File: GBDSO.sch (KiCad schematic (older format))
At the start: 71 parts, among them J1 MJ-3523-SMT-TR, J2 MJ-3523-SMT-TR, J3 Conn_01x32, P1 100k, P2 100k, SW1 SW_SPDT, SW2 SW_SPDT, U1 TL062, U2 DS1267_SOIC, U3 TL062, U4 MAX114CAG, U5 74HC175D, U6 74HC138D, U7 AT27C256R, U8 TLC272, U9 MAX828

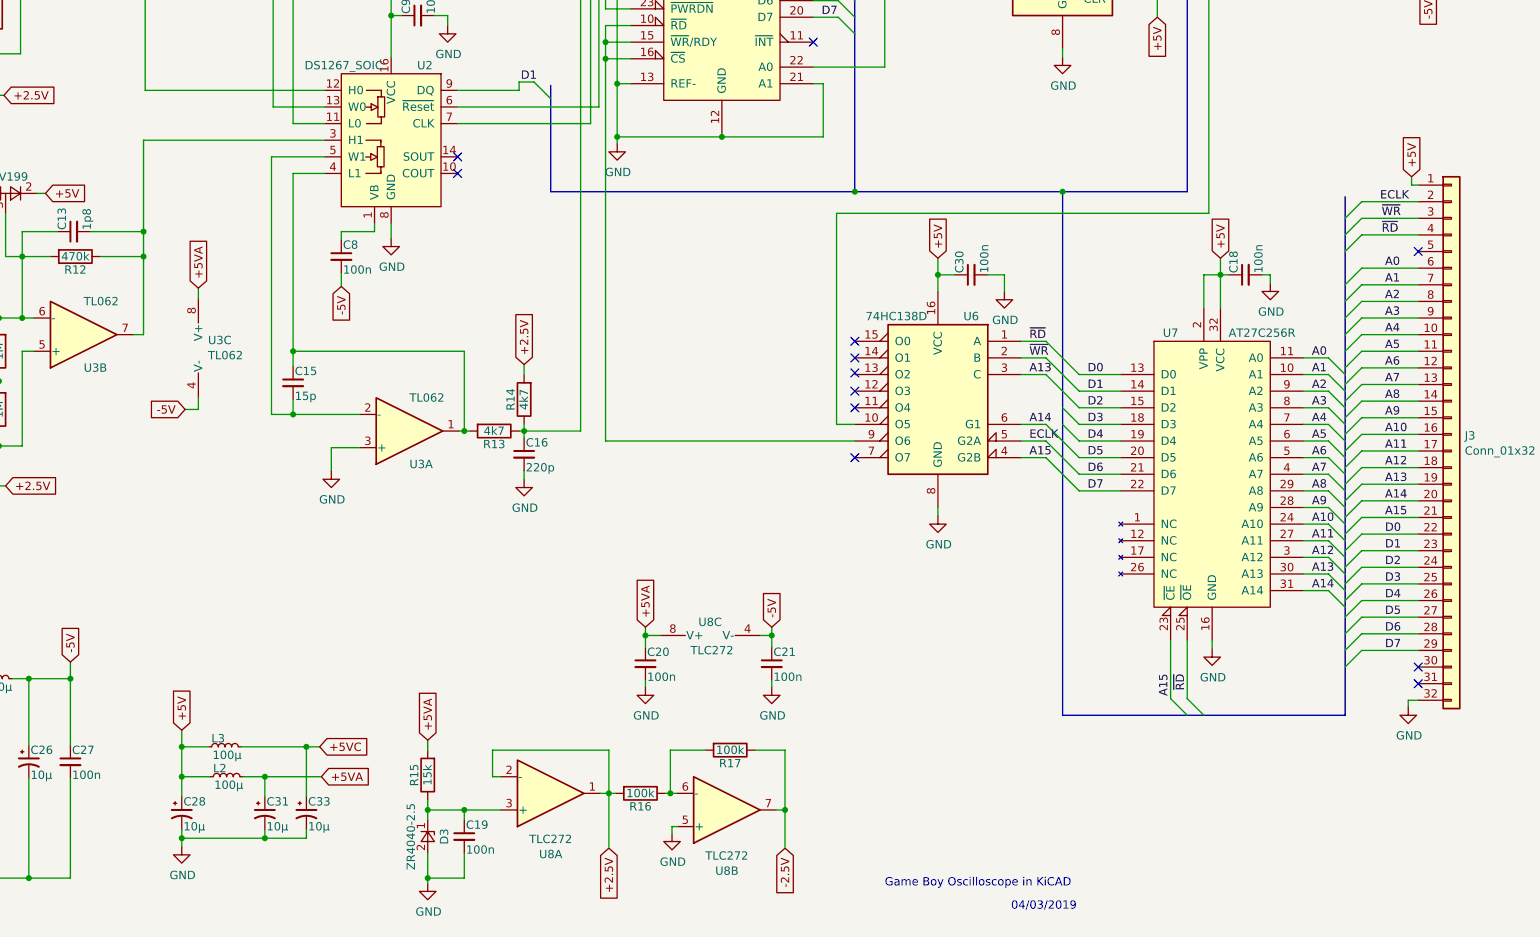
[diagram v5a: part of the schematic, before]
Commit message: added jumpers to the schematic and pcb so that the EPROM can be programmed on the cartridge
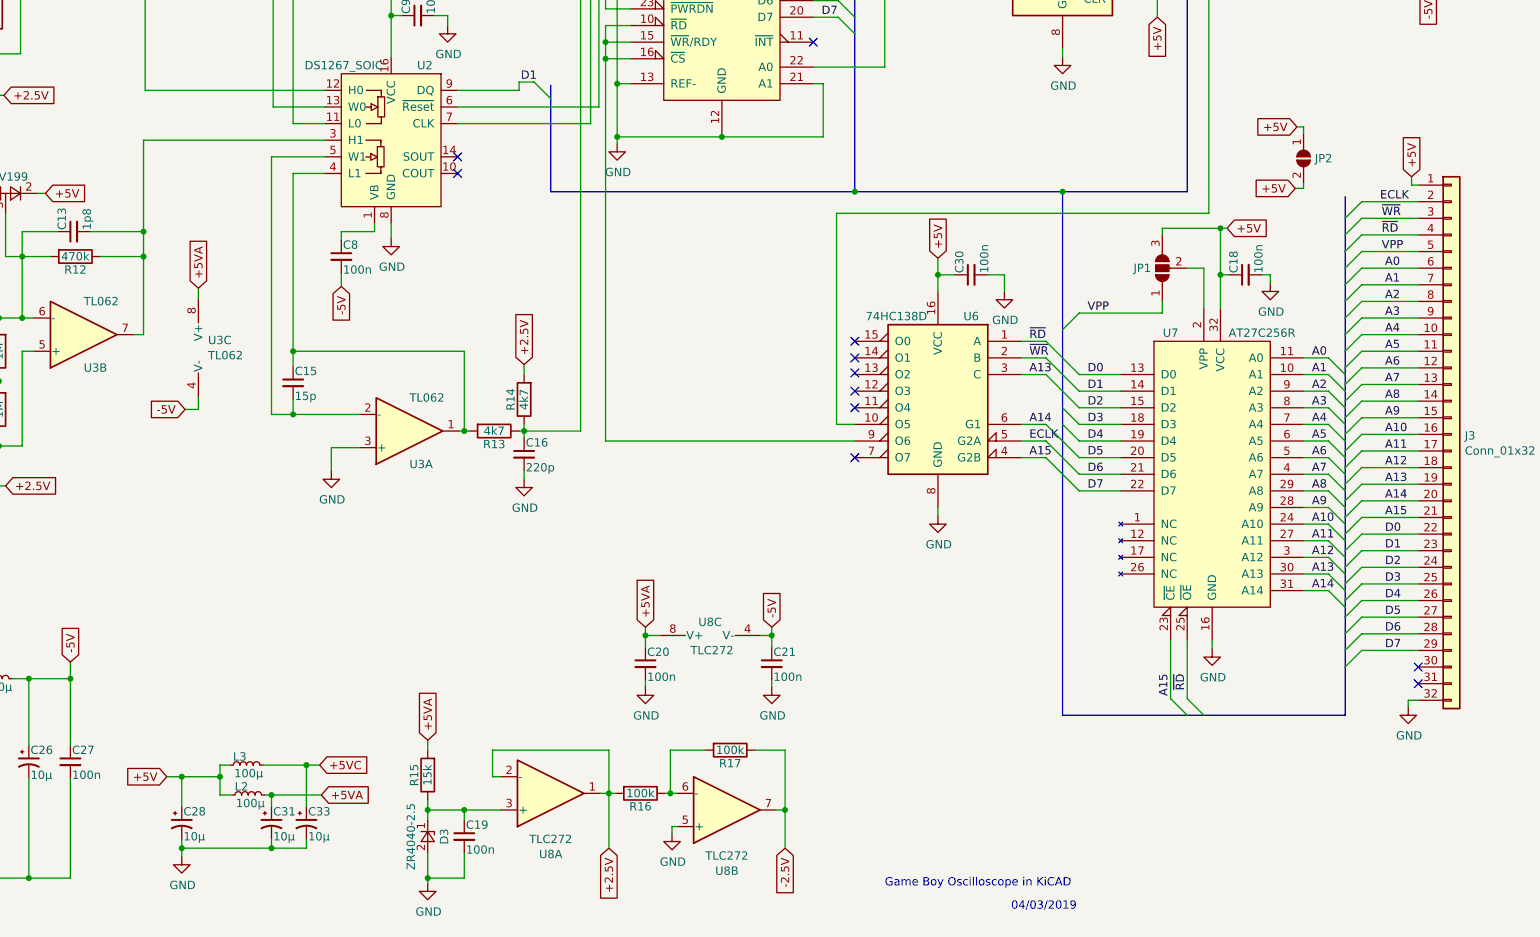
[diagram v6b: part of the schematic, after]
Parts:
- added JP1: SolderJumper_3_Open, Jumper:SolderJumper-3_P1.3mm_Open_RoundedPad1.0x1.5mm_NumberLabels, symbol Jumper:SolderJumper_3_Open
- added JP2: SolderJumper_2_Open, Jumper:SolderJumper-2_P1.3mm_Open_TrianglePad1.0x1.5mm, symbol Jumper:SolderJumper_2_Open
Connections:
- net +5V: now also JP1.3 (B), JP2.1 (A), JP2.2 (B); no longer U7.2 (VPP)
- net VPP: now reaches J3.5 (Pin_5)
- net VPP: now also JP1.1 (A)
- new net: JP1.2 (C), U7.2 (VPP)
- no-connect marks 18 -> 17
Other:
- moved on the sheet: C28, C31, C33, L2, L3
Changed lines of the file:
@@
 L Device:CP1_Small C28
 U 1 1 5C618C17
-P 3150 7050
-F 0 "C28" H 3160 7120 50  0000 L CNN
-F 1 "10µ" H 3160 6970 50  0000 L CNN
-F 2 "Capacitor_SMD:C_1206_3216Metric" H 3150 7050 50  0001 C CNN
-F 3 "" H 3150 7050 50  0001 C CNN
-	1    3150 7050
+P 3150 7110
+F 0 "C28" H 3160 7180 50  0000 L CNN
+F 1 "10µ" H 3160 7030 50  0000 L CNN
+F 2 "Capacitor_SMD:C_1206_3216Metric" H 3150 7110 50  0001 C CNN
+F 3 "" H 3150 7110 50  0001 C CNN
+	1    3150 7110
 	1    0    0    -1
 $EndComp
@@
 L Device:CP1_Small C31
 U 1 1 5C618CCF
-P 3650 7050
-F 0 "C31" H 3660 7120 50  0000 L CNN
-F 1 "10µ" H 3660 6970 50  0000 L CNN
-F 2 "Capacitor_SMD:C_1206_3216Metric" H 3650 7050 50  0001 C CNN
-F 3 "" H 3650 7050 50  0001 C CNN
-	1    3650 7050
+P 3690 7110
+F 0 "C31" H 3700 7180 50  0000 L CNN
+F 1 "10µ" H 3700 7030 50  0000 L CNN
+F 2 "Capacitor_SMD:C_1206_3216Metric" H 3690 7110 50  0001 C CNN
+F 3 "" H 3690 7110 50  0001 C CNN
+	1    3690 7110
 	1    0    0    -1
 $EndComp
@@
 L Device:CP1_Small C33
 U 1 1 5C618D96
-P 3900 7050
-F 0 "C33" H 3910 7120 50  0000 L CNN
-F 1 "10µ" H 3910 6970 50  0000 L CNN
-F 2 "Capacitor_SMD:C_1206_3216Metric" H 3900 7050 50  0001 C CNN
-F 3 "" H 3900 7050 50  0001 C CNN
-	1    3900 7050
+P 3900 7110
+F 0 "C33" H 3910 7180 50  0000 L CNN
+F 1 "10µ" H 3910 7030 50  0000 L CNN
+F 2 "Capacitor_SMD:C_1206_3216Metric" H 3900 7110 50  0001 C CNN
+F 3 "" H 3900 7110 50  0001 C CNN
+	1    3900 7110
 	1    0    0    -1
 $EndComp
@@
 L Device:L_Small L2
 U 1 1 5C619CA4
-P 3420 6830
-F 0 "L2" V 3470 6830 50  0000 L CNN
-F 1 "100µ" V 3370 6730 50  0000 L CNN
-F 2 "Inductor_SMD:L_1206_3216Metric" H 3420 6830 50  0001 C CNN
-F 3 "" H 3420 6830 50  0001 C CNN
-	1    3420 6830
+P 3550 6940
+F 0 "L2" V 3600 6940 50  0000 L CNN
+F 1 "100µ" V 3500 6840 50  0000 L CNN
+F 2 "Inductor_SMD:L_1206_3216Metric" H 3550 6940 50  0001 C CNN
+F 3 "" H 3550 6940 50  0001 C CNN
+	1    3550 6940
 	0    -1   -1   0
 $EndComp
@@
 L Device:L_Small L3
 U 1 1 5C619D6A
-P 3410 6650
-F 0 "L3" V 3460 6650 50  0000 L CNN
-F 1 "100µ" V 3360 6550 50  0000 L CNN
-F 2 "Inductor_SMD:L_1206_3216Metric" H 3410 6650 50  0001 C CNN
-F 3 "" H 3410 6650 50  0001 C CNN
-	1    3410 6650
+P 3540 6760
+F 0 "L3" V 3590 6760 50  0000 L CNN
+F 1 "100µ" V 3490 6660 50  0000 L CNN
+F 2 "Inductor_SMD:L_1206_3216Metric" H 3540 6760 50  0001 C CNN
+F 3 "" H 3540 6760 50  0001 C CNN
+	1    3540 6760
 	0    -1   -1   0
 $EndComp
@@
 	9400 3810 9400 4010
 Wire Wire Line
-	9300 3810 9400 3810
-Wire Wire Line
-	9300 3810 9300 4010
-Wire Wire Line
-	3510 6650 3900 6650
-Wire Wire Line
-	3900 6650 3900 6950
-Wire Wire Line
-	3150 7150 3150 7200
-Wire Wire Line
-	3150 7200 3650 7200
-Wire Wire Line
-	3650 7200 3650 7150
+	3640 6760 3900 6760
+Wire Wire Line
+	3900 6760 3900 7010
+Wire Wire Line
+	3150 7210 3150 7260
+Wire Wire Line
+	3150 7260 3690 7260
+Wire Wire Line
+	3690 7260 3690 7210
 $Comp
 L power:GND #PWR0106
 U 1 1 5C6DF12D
-P 3150 7250
-F 0 "#PWR0106" H 3150 7000 50  0001 C CNN
-F 1 "GND" H 3155 7077 50  0000 C CNN
-F 2 "" H 3150 7250 50  0001 C CNN
-F 3 "" H 3150 7250 50  0001 C CNN
-	1    3150 7250
-	1    0    0    -1
-$EndComp
-Wire Wire Line
-	3150 7250 3150 7200
-Connection ~ 3150 7200
-Wire Wire Line
-	3310 6650 3150 6650
-Wire Wire Line
-	3650 7200 3900 7200
-Wire Wire Line
-	3900 7200 3900 7150
-Connection ~ 3650 7200
-Connection ~ 3150 6650
-Connection ~ 3900 6650
+P 3150 7310
+F 0 "#PWR0106" H 3150 7060 50  0001 C CNN
+F 1 "GND" H 3155 7137 50  0000 C CNN
+F 2 "" H 3150 7310 50  0001 C CNN
+F 3 "" H 3150 7310 50  0001 C CNN
+	1    3150 7310
+	1    0    0    -1
+$EndComp
+Wire Wire Line
+	3150 7310 3150 7260
+Connection ~ 3150 7260
+Wire Wire Line
+	3690 7260 3900 7260
+Wire Wire Line
+	3900 7260 3900 7210
+Connection ~ 3690 7260
+Connection ~ 3900 6760
 Text GLabel 630  6140 1    50   Input ~ 0
 +5V
@@
 Wire Wire Line
 	2480 6140 2480 6240
-Text GLabel 3150 6550 1    50   Input ~ 0
+Text GLabel 3060 6830 0    50   Input ~ 0
 +5V
-Wire Wire Line
-	3150 6550 3150 6650
-Text GLabel 3990 6830 2    50   Input ~ 0
+Text GLabel 3990 6940 2    50   Input ~ 0
 +5VA
-Text GLabel 3980 6650 2    50   Input ~ 0
+Text GLabel 3980 6760 2    50   Input ~ 0
 +5VC
 Wire Wire Line
-	3980 6650 3900 6650
-Text GLabel 9400 3710 1    50   Input ~ 0
+	3980 6760 3900 6760
+Text GLabel 9440 3530 2    50   Input ~ 0
 +5V
-Wire Wire Line
-	9400 3710 9400 3810
 Wire Wire Line
 	7800 3810 7700 3810
@@
 Connection ~ 6780 7030
 Wire Wire Line
-	3150 6650 3150 6830
-Wire Wire Line
-	3520 6830 3650 6830
-Wire Wire Line
-	3320 6830 3150 6830
-Connection ~ 3150 6830
-Wire Wire Line
-	3150 6830 3150 6950
-Wire Wire Line
-	3650 6830 3650 6950
-Connection ~ 3650 6830
-Wire Wire Line
-	3650 6830 3990 6830
+	3650 6940 3690 6940
+Wire Wire Line
+	3690 6940 3690 7010
+Connection ~ 3690 6940
+Wire Wire Line
+	3690 6940 3990 6940
 Text GLabel 1660 5080 0    50   Input ~ 0
 -2.5V
@@
 NoConn ~ 10590 6270
 NoConn ~ 10590 6170
-NoConn ~ 10590 3670
 $Comp
 L Amplifier_Operational:TL062 U1
@@
 Text Notes 8140 7640 0    50   ~ 0
 04/03/2019
+$Comp
+L Jumper:SolderJumper_3_Open JP1
+U 1 1 5C86EAD3
+P 9050 3770
+F 0 "JP1" V 9050 3838 50  0000 L CNN
+F 1 "SolderJumper_3_Open" V 9005 3838 50  0001 L CNN
+F 2 "Jumper:SolderJumper-3_P1.3mm_Open_RoundedPad1.0x1.5mm_NumberLabels" H 9050 3770 50  0001 C CNN
+F 3 "~" H 9050 3770 50  0001 C CNN
+	1    9050 3770
+	0    -1   -1   0
+$EndComp
+Entry Wire Line
+	8450 4140 8550 4040
+Wire Wire Line
+	9440 3530 9400 3530
+Wire Wire Line
+	9400 3530 9400 3810
+Wire Wire Line
+	9400 3530 9050 3530
+Wire Wire Line
+	9050 3530 9050 3570
+Connection ~ 9400 3530
+Wire Wire Line
+	9200 3770 9300 3770
+Wire Wire Line
+	9300 3770 9300 4010
+Text Label 8600 4040 0    50   ~ 0
+VPP
+Entry Wire Line
+	10150 3770 10250 3670
+Wire Wire Line
+	10250 3670 10590 3670
+Text Label 10370 3670 0    50   ~ 0
+VPP
+Wire Wire Line
+	8550 4040 9050 4040
+Wire Wire Line
+	9050 3970 9050 4040
+$Comp
+L Jumper:SolderJumper_2_Open JP2
+U 1 1 5CAD1655
+P 9900 3110
+F 0 "JP2" V 9900 3178 50  0000 L CNN
+F 1 "SolderJumper_2_Open" V 9945 3178 50  0001 L CNN
+F 2 "Jumper:SolderJumper-2_P1.3mm_Open_TrianglePad1.0x1.5mm" H 9900 3110 50  0001 C CNN
+F 3 "~" H 9900 3110 50  0001 C CNN
+	1    9900 3110
+	0    1    1    0
+$EndComp
+Wire Wire Line
+	3150 6830 3380 6830
+Wire Wire Line
+	3380 6830 3380 6760
+Wire Wire Line
+	3380 6760 3440 6760
+Wire Wire Line
+	3380 6830 3380 6940
+Wire Wire Line
+	3380 6940 3450 6940
+Connection ~ 3380 6830
+Wire Wire Line
+	3150 6830 3150 7010
+Wire Wire Line
+	3150 6830 3060 6830
+Connection ~ 3150 6830
+Text GLabel 9850 3290 0    50   Input ~ 0
++5V
+Wire Wire Line
+	9850 3290 9900 3290
+Wire Wire Line
+	9900 3290 9900 3260
+Text GLabel 9860 2920 0    50   Input ~ 0
++5V
+Wire Wire Line
+	9860 2920 9900 2920
+Wire Wire Line
+	9900 2920 9900 2960
 Wire Bus Line
 	5370 2670 5370 3310
@@
 	9200 1250 9200 3310
 Wire Bus Line
+	8450 3310 8450 6460
+Wire Bus Line
 	7200 1560 7200 3310
 Wire Bus Line
-	8450 3310 8450 6460
-Wire Bus Line
 	10150 3340 10150 6460

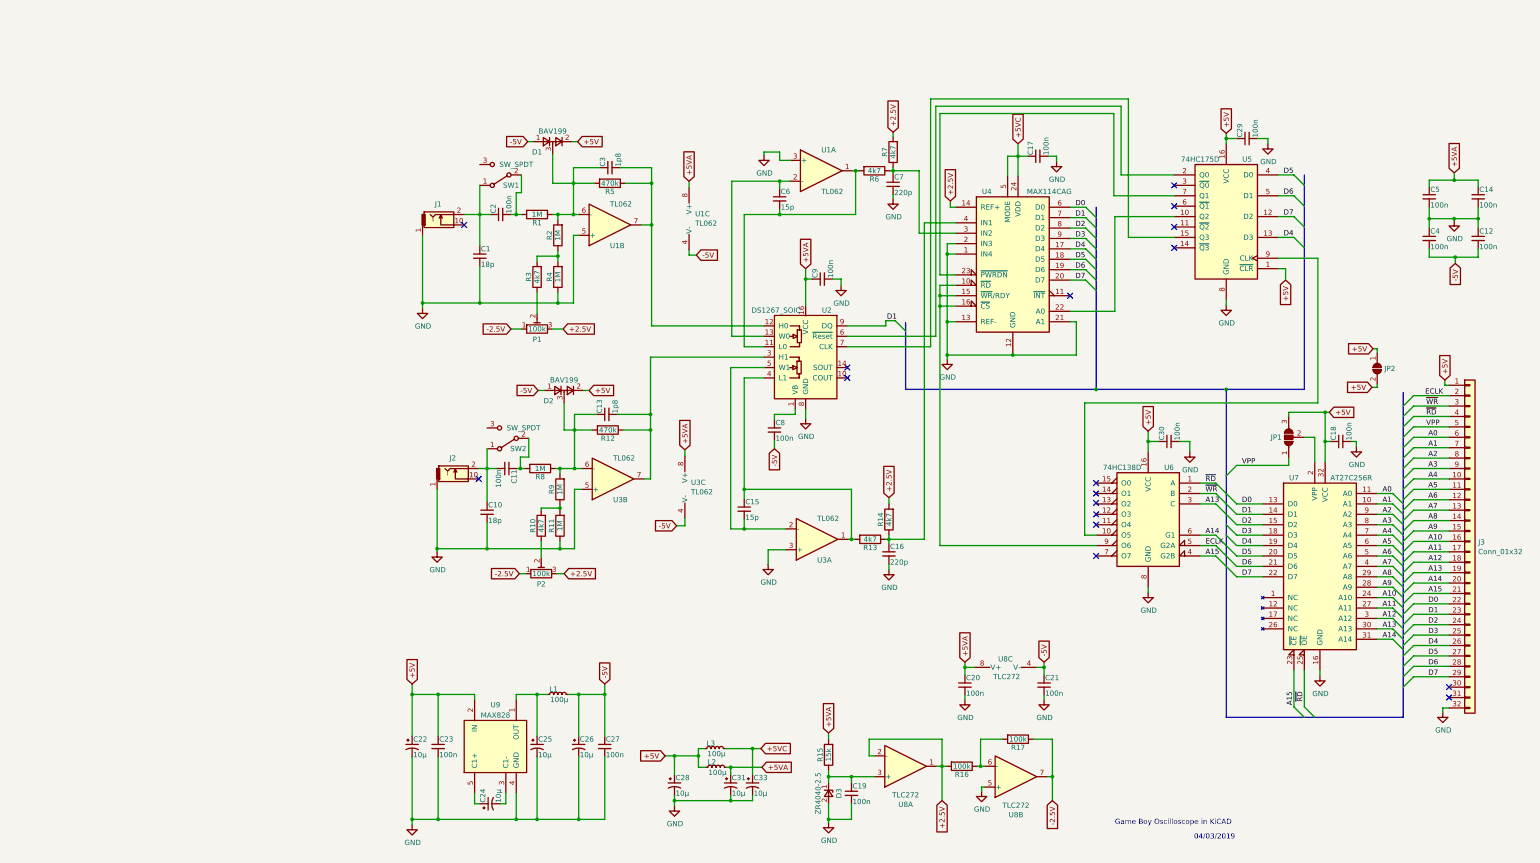
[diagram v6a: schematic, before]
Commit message: updated schematic (now 2 pages) and PCB + adding Gekkio DS Lite footprint
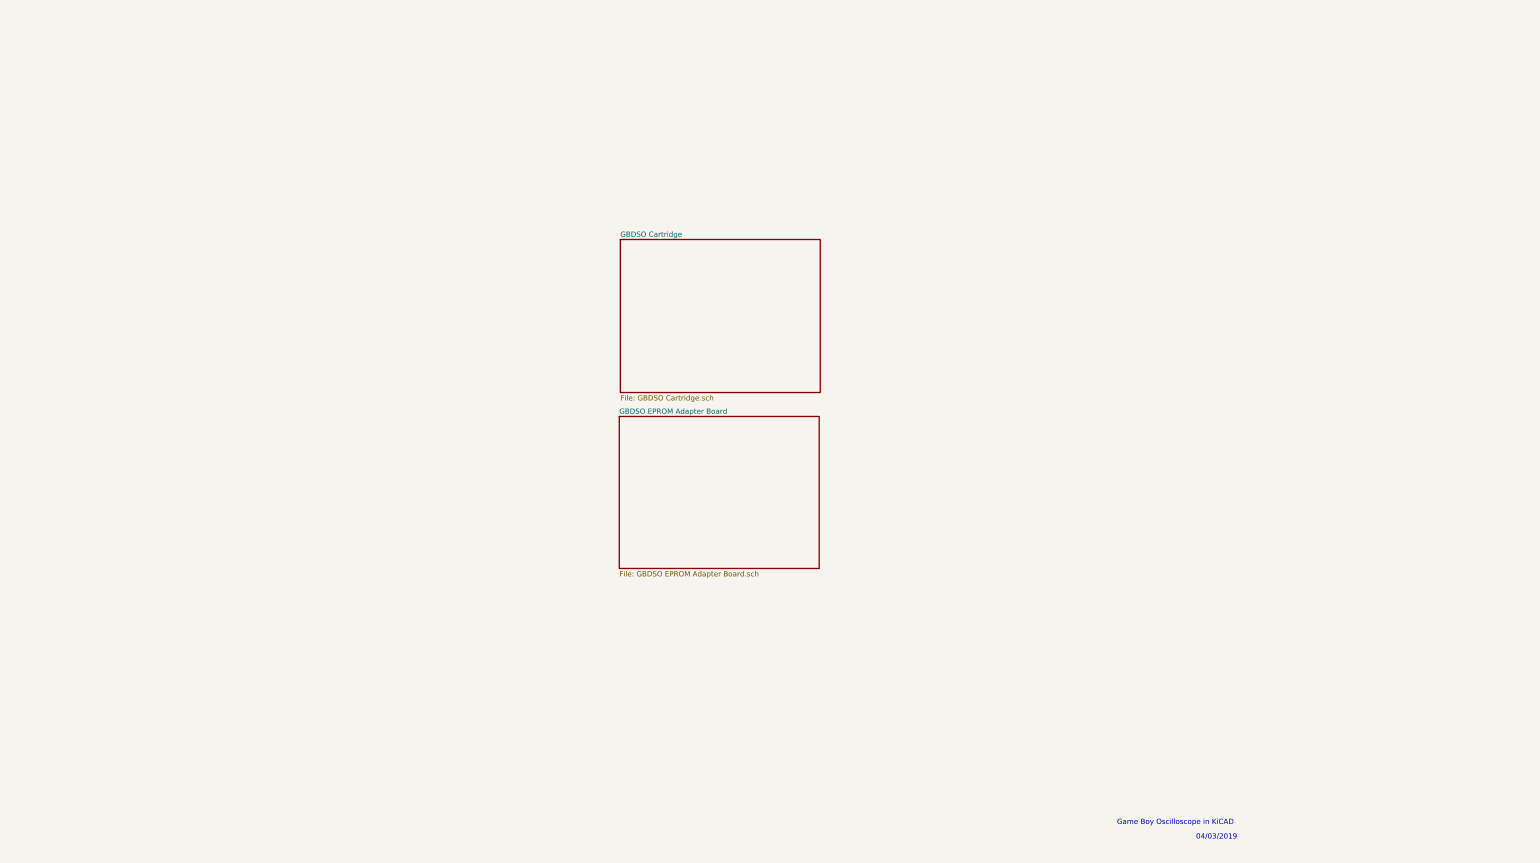
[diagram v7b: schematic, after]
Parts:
- removed C1, C10: 18p, Capacitor_SMD:C_0805_2012Metric, symbol Device:C_Small
- removed C11, C12, C14, C17, C18, C19, C2, C20, C21, C23, C27, C29, C30, C4, C5, C8, C9: 100n, Capacitor_SMD:C_0805_2012Metric, symbol Device:C_Small
- removed C13, C3: 1p8, Capacitor_SMD:C_0805_2012Metric, symbol Device:C_Small
- removed C15, C6: 15p, Capacitor_SMD:C_0805_2012Metric, symbol Device:C_Small
- removed C16, C7: 220p, Capacitor_SMD:C_0805_2012Metric, symbol Device:C_Small
- removed C22, C24, C25, C26, C28, C31, C33: 10µ, Capacitor_SMD:C_1206_3216Metric, symbol Device:CP1_Small
- removed D1, D2: BAV199, Package_TO_SOT_SMD:SOT-23_Handsoldering, symbol BAV199:BAV199
- removed D3: ZR4040-2.5, Package_TO_SOT_SMD:SOT-23_Handsoldering, symbol ZR40402F25TA:ZR4040-2.5
- removed J1, J2: MJ-3523-SMT-TR, MJ-3523-SMT-TR:MJ-3523-SMT-TR, symbol MJ-3523-SMT-TR:MJ-3523-SMT-TR
- removed J3: Conn_01x32, GB_EdgeConnector:GB_EdgeConnector, symbol Connector_Generic:Conn_01x32
- removed JP1: SolderJumper_3_Open, Jumper:SolderJumper-3_P1.3mm_Open_RoundedPad1.0x1.5mm_NumberLabels, symbol Jumper:SolderJumper_3_Open
- removed JP2: SolderJumper_2_Open, Jumper:SolderJumper-2_P1.3mm_Open_TrianglePad1.0x1.5mm, symbol Jumper:SolderJumper_2_Open
- removed L1, L2, L3: 100µ, Inductor_SMD:L_1206_3216Metric, symbol Device:L_Small
- removed P1, P2: 100k, Potentiometer_SMD:Potentiometer_Vishay_TS53YJ_Vertical, symbol Device:R_POT_TRIM
- removed R1, R11, R2, R4, R8, R9: 1M, Resistor_SMD:R_0805_2012Metric, symbol Device:R
- removed R10, R13, R14, R3, R6, R7: 4k7, Resistor_SMD:R_0805_2012Metric, symbol Device:R
- removed R12, R5: 470k, Resistor_SMD:R_0805_2012Metric, symbol Device:R
- removed R15: 15k, Resistor_SMD:R_0805_2012Metric, symbol Device:R
- removed R16, R17: 100k, Resistor_SMD:R_0805_2012Metric, symbol Device:R
- removed SW1, SW2: SW_SPDT, Button_Switch_SMD:SW_SPDT_CK-JS102011SAQN, symbol Switch:SW_SPDT
- removed U1, U3: TL062, Package_SO:SO-8_5.3x6.2mm_P1.27mm, symbol Amplifier_Operational:TL062
- removed U2: DS1267_SOIC, Package_SO:SOIC-16_3.9x9.9mm_P1.27mm, symbol Potentiometer_Digital:DS1267_SOIC
- removed U4: MAX114CAG, Package_SO:SSOP-24_3.9x8.7mm_P0.635mm, symbol MAX114CAG:MAX114CAG
- removed U5: 74HC175D, Package_SO:SOIC-16_3.9x9.9mm_P1.27mm, symbol 74HC175D:74HC175D
- removed U6: 74HC138D, Package_SO:SOIC-16_3.9x9.9mm_P1.27mm, symbol 74HC138D:74HC138D
- removed U7: AT27C256R, Package_LCC:PLCC-32_11.4x14.0mm_P1.27mm, symbol AT27C256R:AT27C256R
- removed U8: TLC272, Package_SO:SOIC-8_3.9x4.9mm_P1.27mm, symbol Amplifier_Operational:TLC272
- removed U9: MAX828, Package_TO_SOT_SMD:SOT-23-5_HandSoldering, symbol MAX828EUK:MAX828
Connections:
- no-connect marks 17 -> 0
